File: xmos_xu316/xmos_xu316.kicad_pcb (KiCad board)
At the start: 6 copper layers, 50 x 50 mm, 93 parts, among them CN1 PJ-327A0-SMT, J1 Conn_02x14_Odd_Even, J2 Conn_02x14_Odd_Even, J3 USB_C_Receptacle_USB2.0_16P, U1 XU316-1024-QF60B-C24, U10 SN74AVC4T774PWR, U11 CS43131-CNZR, U12 NZ2520SDA-24.576MHZ, U13 PCA9306DCUR, U2 USB6B1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

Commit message: fixed pcb errors
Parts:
- added R19: 1M, Resistor_SMD:R_0603_1608Metric, F.Cu at (156.0, 87.2)
- C1, C2: value 10pF -> 22pF
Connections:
- J2 pad 2: /xu316/X1D11 -> /xu316/X1D09
- U1 pad 11: MCU_MCLK -> /xu316/X1D09
- U1 pad 14: /xu316/X1D11 -> MCU_MCLK
- U10 pad 3: MCU_MCLK -> /xu316/X1D09
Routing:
- net /xu316/X1D09: track 0.00 -> 67.2 mm, vias 0 -> 2
- net /xu316/X1D11: track 31.2 -> 0.00 mm, vias 1 -> 0
- net MCU_MCLK: track 67.1 -> 36.4 mm, vias 2 -> 1
- net /xu316/HSE_IN: track 7.90 -> 9.88 mm

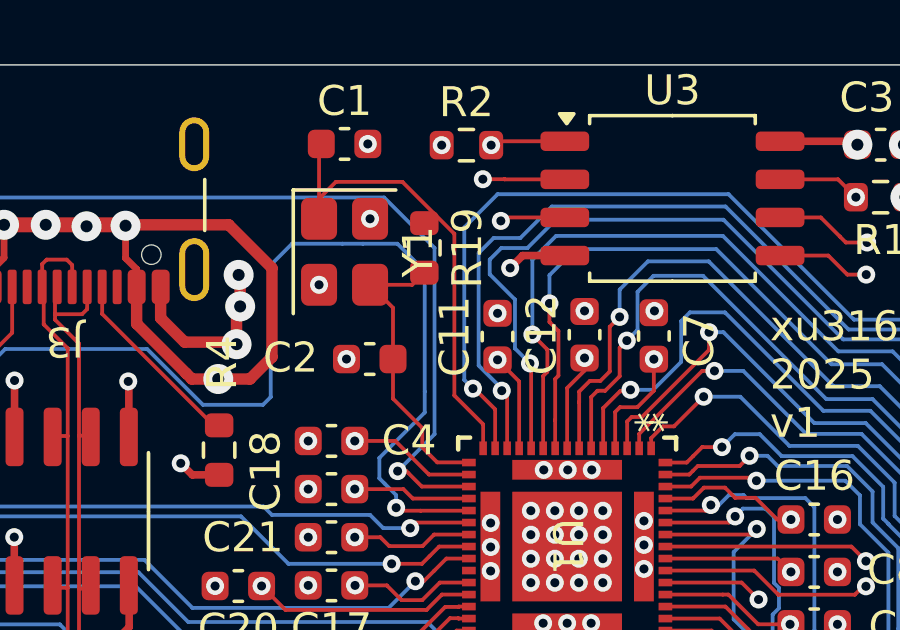
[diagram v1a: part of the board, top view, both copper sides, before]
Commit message: fixed one more error(SN74AVC4T774)
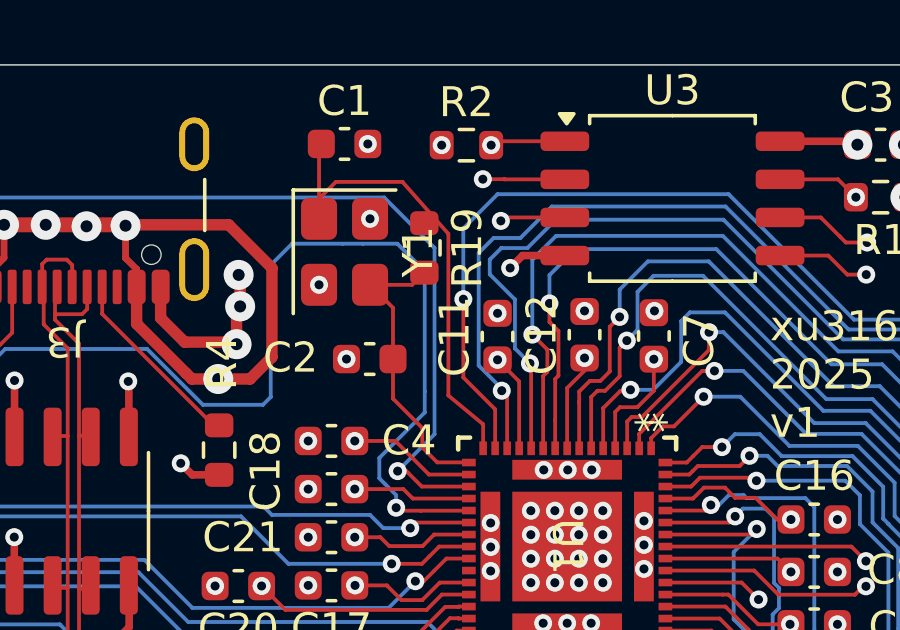
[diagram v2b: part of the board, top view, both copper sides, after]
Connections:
- U10 pad 3: /xu316/X1D09 -> MCU_MCLK
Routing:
- net /xu316/X1D09: track 67.2 -> 29.0 mm, vias 2 -> 1
- net MCU_MCLK: track 36.4 -> 73.3 mm, vias 1 -> 2
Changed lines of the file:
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@@
 			(size 1.778 0.3556)
 			(layers "F.Cu" "F.Mask" "F.Paste")
-			(net 29 "/xu316/X1D09")
+			(net 66 "MCU_MCLK")
 			(pinfunction "A1")
 			(pintype "bidirectional")
@@
 	)
 	(segment
-		(start 157 86.72)
+		(start 156.8 86.72)
 		(end 155.27 84.99)
 		(width 0.127)
@@
 	)
 	(segment
-		(start 157 92.11)
-		(end 157 86.72)
+		(start 156.8 92.11)
+		(end 156.8 86.72)
 		(width 0.127)
 		(layer "F.Cu")
@@
 	(segment
 		(start 157.95935 93.06935)
-		(end 157 92.11)
+		(end 156.8 92.11)
 		(width 0.127)
 		(layer "F.Cu")
@@
 	)
 	(segment
-		(start 138.2688 111.414801)
-		(end 141.465199 111.414801)
-		(width 0.127)
-		(layer "F.Cu")
-		(net 29)
-	)
-	(segment
 		(start 159.55955 91.07955)
 		(end 159.55955 93.870102)
@@
 		(net 29)
 	)
-	(segment
-		(start 141.465199 111.414801)
-		(end 141.55 111.33)
-		(width 0.127)
-		(layer "F.Cu")
-		(net 29)
-	)
 	(via
 		(at 159.52 91.04)
@@
 		(net 29)
 	)
-	(via
-		(at 141.55 111.33)
-		(size 0.6)
-		(drill 0.3)
-		(layers "F.Cu" "B.Cu")
-		(net 29)
-	)
 	(segment
 		(start 159.02 90.54)
@@
 	)
 	(segment
-		(start 146.52 96.87)
-		(end 146.52 109.17)
-		(width 0.127)
-		(layer "In2.Cu")
-		(net 29)
-	)
-	(segment
-		(start 149.39 94)
-		(end 146.52 96.87)
-		(width 0.127)
-		(layer "In2.Cu")
-		(net 29)
-	)
-	(segment
-		(start 149.39 92.81)
-		(end 149.39 94)
-		(width 0.127)
-		(layer "In2.Cu")
-		(net 29)
-	)
-	(segment
-		(start 157.18 90.22)
-		(end 155.71 91.69)
-		(width 0.127)
-		(layer "In2.Cu")
-		(net 29)
-	)
-	(segment
-		(start 158.63 90.22)
-		(end 157.18 90.22)
-		(width 0.127)
-		(layer "In2.Cu")
-		(net 29)
-	)
-	(segment
-		(start 144.36 111.33)
-		(end 141.55 111.33)
-		(width 0.127)
-		(layer "In2.Cu")
-		(net 29)
-	)
-	(segment
 		(start 159.52 91.04)
 		(end 159.45 91.04)
@@
 	)
 	(segment
-		(start 146.52 109.17)
-		(end 144.36 111.33)
-		(width 0.127)
-		(layer "In2.Cu")
-		(net 29)
-	)
-	(segment
-		(start 150.51 91.69)
-		(end 149.39 92.81)
-		(width 0.127)
-		(layer "In2.Cu")
-		(net 29)
-	)
-	(segment
-		(start 155.71 91.69)
-		(end 150.51 91.69)
-		(width 0.127)
-		(layer "In2.Cu")
-		(net 29)
-	)
-	(segment
-		(start 159.45 91.04)
-		(end 158.63 90.22)
-		(width 0.127)
-		(layer "In2.Cu")
-		(net 29)
-	)
-	(segment
 		(start 155.47 94.7)
 		(end 155.4 94.63)
@@
 	)
 	(segment
+		(start 157.3 91.51)
+		(end 157.3 88.9)
+		(width 0.127)
+		(layer "F.Cu")
+		(net 66)
+	)
+	(segment
+		(start 138.2688 111.414801)
+		(end 141.465199 111.414801)
+		(width 0.127)
+		(layer "F.Cu")
+		(net 66)
+	)
+	(segment
 		(start 158.3594 92.5694)
-		(end 158.3594 93.870102)
+		(end 157.3 91.51)
 		(width 0.127)
 		(layer "F.Cu")
@@
 	)
 	(segment
-		(start 157.62 91.88)
-		(end 157.67 91.88)
+		(start 141.465199 111.414801)
+		(end 141.55 111.33)
 		(width 0.127)
 		(layer "F.Cu")
@@
 	)
 	(segment
-		(start 157.67 91.88)
+		(start 158.3594 93.870102)
 		(end 158.3594 92.5694)
 		(width 0.127)
@@
 	)
 	(via
-		(at 157.62 91.88)
+		(at 141.55 111.33)
 		(size 0.6)
 		(drill 0.3)
@@
 		(net 66)
 	)
+	(via
+		(at 157.3 88.9)
+		(size 0.6)
+		(drill 0.3)
+		(layers "F.Cu" "B.Cu")
+		(free yes)
+		(net 66)
+	)
 	(segment
-		(start 178.5 88.1545)
-		(end 178.5 90.82)
+		(start 166.14 85.4)
+		(end 170.32 89.58)
 		(width 0.127)
 		(layer "B.Cu")
@@
 	)
 	(segment
-		(start 178.5 90.82)
-		(end 177.2 92.12)
+		(start 170.32 89.58)
+		(end 172.04 89.58)
 		(width 0.127)
 		(layer "B.Cu")
@@
 	)
 	(segment
-		(start 157.33 86.51)
-		(end 158.44 85.4)
+		(start 174 87.9)
+		(end 178.2455 87.9)
 		(width 0.127)
 		(layer "B.Cu")
@@
 	)
 	(segment
-		(start 157.33 91.59)
-		(end 157.33 86.51)
+		(start 157.3 86.54)
+		(end 158.44 85.4)
 		(width 0.127)
 		(layer "B.Cu")
@@
 	)
 	(segment
-		(start 170.32 89.58)
-		(end 172.04 89.58)
+		(start 172.04 89.58)
+		(end 174 87.9)
 		(width 0.127)
 		(layer "B.Cu")
@@
 	)
 	(segment
-		(start 174 87.9)
-		(end 178.2455 87.9)
+		(start 178.5 88.1545)
+		(end 178.5 90.82)
 		(width 0.127)
 		(layer "B.Cu")
@@
 	)
 	(segment
-		(start 178.2455 87.9)
-		(end 178.5 88.1545)
+		(start 157.3 88.9)
+		(end 157.3 86.54)
 		(width 0.127)
 		(layer "B.Cu")
@@
 	)
 	(segment
-		(start 166.14 85.4)
-		(end 170.32 89.58)
+		(start 178.2455 87.9)
+		(end 178.5 88.1545)
 		(width 0.127)
 		(layer "B.Cu")
@@
 	)
 	(segment
-		(start 157.62 91.88)
-		(end 157.33 91.59)
+		(start 178.5 90.82)
+		(end 177.2 92.12)
 		(width 0.127)
 		(layer "B.Cu")
@@
 	)
 	(segment
-		(start 172.04 89.58)
-		(end 174 87.9)
+		(start 157.3 89.92)
+		(end 157.3 88.9)
 		(width 0.127)
-		(layer "B.Cu")
+		(layer "In2.Cu")
+		(net 66)
+	)
+	(segment
+		(start 146.52 96.87)
+		(end 146.52 109.17)
+		(width 0.127)
+		(layer "In2.Cu")
+		(net 66)
+	)
+	(segment
+		(start 149.39 94)
+		(end 146.52 96.87)
+		(width 0.127)
+		(layer "In2.Cu")
+		(net 66)
+	)
+	(segment
+		(start 149.39 92.81)
+		(end 149.39 94)
+		(width 0.127)
+		(layer "In2.Cu")
+		(net 66)
+	)
+	(segment
+		(start 144.36 111.33)
+		(end 141.55 111.33)
+		(width 0.127)
+		(layer "In2.Cu")
+		(net 66)
+	)
+	(segment
+		(start 146.52 109.17)
+		(end 144.36 111.33)
+		(width 0.127)
+		(layer "In2.Cu")
+		(net 66)
+	)
+	(segment
+		(start 150.51 91.69)
+		(end 149.39 92.81)
+		(width 0.127)
+		(layer "In2.Cu")
+		(net 66)
+	)
+	(segment
+		(start 155.71 91.69)
+		(end 150.51 91.69)
+		(width 0.127)
+		(layer "In2.Cu")
+		(net 66)
+	)
+	(segment
+		(start 155.71 91.69)
+		(end 157.3 89.92)
+		(width 0.127)
+		(layer "In2.Cu")
 		(net 66)
 	)

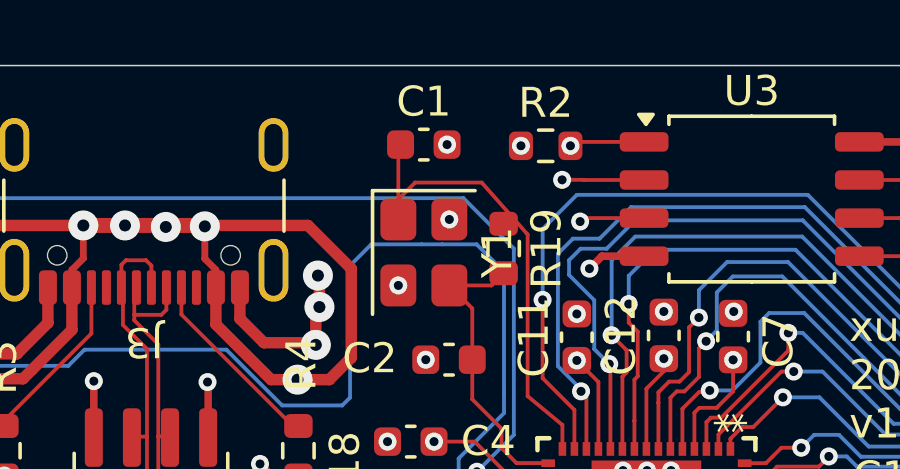
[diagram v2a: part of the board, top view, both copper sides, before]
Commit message: add rd for HSE
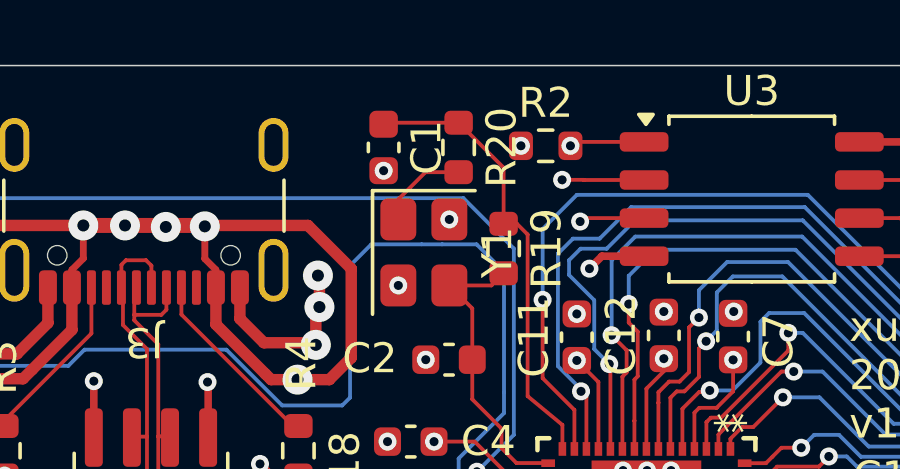
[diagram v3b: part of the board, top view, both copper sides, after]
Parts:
- added R20: 680, Resistor_SMD:R_0603_1608Metric, F.Cu at (154.5, 83.8)
- moved C1 1.34 mm to (152.0, 83.8), turned to -90 degrees
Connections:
- Y1 pad 1: /xu316/HSE_OUT -> Net-(R20-Pad2)
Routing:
- net Net-(R20-Pad2): track 0.00 -> 3.05 mm
- net /xu316/HSE_OUT: track 16.2 -> 15.2 mm
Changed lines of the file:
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@@
 	(net 96 "unconnected-(U11A-DSDCLK{slash}SCLK2-Pad32)")
 	(net 97 "unconnected-(U11A-DDB{slash}LRCK2-Pad29)")
+	(net 98 "Net-(R20-Pad2)")
 	(footprint "Resistor_SMD:R_0603_1608Metric"
 		(layer "F.Cu")
@@
 		)
 	)
+	(footprint "Resistor_SMD:R_0603_1608Metric"
+		(layer "F.Cu")
+		(at 154.5 83.82 -90)
+		(descr "Resistor SMD 0603 (1608 Metric), square (rectangular) end terminal, IPC_7351 nominal, (Body size source: IPC-SM-782 page 72, https://www.pcb-3d.com/wordpress/wp-content/uploads/ipc-sm-782a_amendment_1_and_2.pdf), generated with kicad-footprint-generator")
+		(tags "resistor")
+		(property "Reference" "R20"
+			(at 0 -1.43 90)
+			(layer "F.SilkS")
+			(effects
+				(font
+					(size 1 1)
+					(thickness 0.15)
+				)
+			)
+		)
+		(property "Value" "680"
+			(at 0 1.43 90)
+			(layer "F.Fab")
+			(effects
+				(font
+					(size 1 1)
+					(thickness 0.15)
+				)
+			)
+		)
+		(property "Datasheet" "~"
+			(at 0 0 90)
+			(layer "F.Fab")
+			(hide yes)
+			(effects
+				(font
+					(size 1.27 1.27)
+					(thickness 0.15)
+				)
+			)
+		)
+		(property "Description" "Resistor"
+			(at 0 0 90)
+			(layer "F.Fab")
+			(hide yes)
+			(effects
+				(font
+					(size 1.27 1.27)
+					(thickness 0.15)
+				)
+			)
+		)
+		(property ki_fp_filters "R_*")
+		(sheetname "/xu316/")
+		(sheetfile "xu316.kicad_sch")
+		(attr smd)
+		(fp_line
+			(start -0.237258 0.5225)
+			(end 0.237258 0.5225)
+			(stroke
+				(width 0.12)
+				(type solid)
+			)
+			(layer "F.SilkS")
+		)
+		(fp_line
+			(start -0.237258 -0.5225)
+			(end 0.237258 -0.5225)
+			(stroke
+				(width 0.12)
+				(type solid)
+			)
+			(layer "F.SilkS")
+		)
+		(fp_line
+			(start -1.48 0.73)
+			(end -1.48 -0.73)
+			(stroke
+				(width 0.05)
+				(type solid)
+			)
+			(layer "F.CrtYd")
+		)
+		(fp_line
+			(start 1.48 0.73)
+			(end -1.48 0.73)
+			(stroke
+				(width 0.05)
+				(type solid)
+			)
+			(layer "F.CrtYd")
+		)
+		(fp_line
+			(start -1.48 -0.73)
+			(end 1.48 -0.73)
+			(stroke
+				(width 0.05)
+				(type solid)
+			)
+			(layer "F.CrtYd")
+		)
+		(fp_line
+			(start 1.48 -0.73)
+			(end 1.48 0.73)
+			(stroke
+				(width 0.05)
+				(type solid)
+			)
+			(layer "F.CrtYd")
+		)
+		(fp_line
+			(start -0.8 0.4125)
+			(end -0.8 -0.4125)
+			(stroke
+				(width 0.1)
+				(type solid)
+			)
+			(layer "F.Fab")
+		)
+		(fp_line
+			(start 0.8 0.4125)
+			(end -0.8 0.4125)
+			(stroke
+				(width 0.1)
+				(type solid)
+			)
+			(layer "F.Fab")
+		)
+		(fp_line
+			(start -0.8 -0.4125)
+			(end 0.8 -0.4125)
+			(stroke
+				(width 0.1)
+				(type solid)
+			)
+			(layer "F.Fab")
+		)
+		(fp_line
+			(start 0.8 -0.4125)
+			(end 0.8 0.4125)
+			(stroke
+				(width 0.1)
+				(type solid)
+			)
+			(layer "F.Fab")
+		)
+		(fp_text user "${REFERENCE}"
+			(at 0 0 90)
+			(layer "F.Fab")
+			(effects
+				(font
+					(size 0.4 0.4)
+					(thickness 0.06)
+				)
+			)
+		)
+		(pad "1" smd roundrect
+			(at -0.825 0 270)
+			(size 0.8 0.95)
+			(layers "F.Cu" "F.Mask" "F.Paste")
+			(roundrect_rratio 0.25)
+			(net 10 "/xu316/HSE_OUT")
+			(pintype "passive")
+		)
+		(pad "2" smd roundrect
+			(at 0.825 0 270)
+			(size 0.8 0.95)
+			(layers "F.Cu" "F.Mask" "F.Paste")
+			(roundrect_rratio 0.25)
+			(net 98 "Net-(R20-Pad2)")
+			(pintype "passive")
+		)
+		(embedded_fonts no)
+		(model "${KICAD6_3DMODEL_DIR}/Resistor_SMD.3dshapes/R_0603_1608Metric.wrl"
+			(offset
+				(xyz 0 0 0)
+			)
+			(scale
+				(xyz 1 1 1)
+			)
+			(rotate
+				(xyz 0 0 0)
+			)
+		)
+	)
 	(footprint "Capacitor_SMD:C_0603_1608Metric"
 		(layer "F.Cu")
@@
 	(footprint "Capacitor_SMD:C_0603_1608Metric"
 		(layer "F.Cu")
-		(at 153.34 83.725)
+		(at 152 83.82 -90)
 		(descr "Capacitor SMD 0603 (1608 Metric), square (rectangular) end terminal, IPC-7351 nominal, (Body size source: IPC-SM-782 page 76, https://www.pcb-3d.com/wordpress/wp-content/uploads/ipc-sm-782a_amendment_1_and_2.pdf), generated with kicad-footprint-generator")
 		(tags "capacitor")
 		(property "Reference" "C1"
-			(at 0 -1.43 0)
+			(at 0 -1.43 90)
 			(layer "F.SilkS")
 			(effects
@@
 		)
 		(property "Value" "22pF"
-			(at 0 1.43 0)
+			(at 0 1.43 90)
 			(layer "F.Fab")
 			(effects
@@
 		)
 		(property "Datasheet" "~"
-			(at 0 0 0)
+			(at 0 0 90)
 			(layer "F.Fab")
 			(hide yes)
@@
 		)
 		(property "Description" "Unpolarized capacitor"
-			(at 0 0 0)
+			(at 0 0 90)
 			(layer "F.Fab")
 			(hide yes)
@@
 		(attr smd)
 		(fp_line
-			(start -0.14058 -0.51)
-			(end 0.14058 -0.51)
+			(start -0.14058 0.51)
+			(end 0.14058 0.51)
 			(stroke
 				(width 0.12)
@@
 		)
 		(fp_line
-			(start -0.14058 0.51)
-			(end 0.14058 0.51)
+			(start -0.14058 -0.51)
+			(end 0.14058 -0.51)
 			(stroke
 				(width 0.12)
@@
 		)
 		(fp_line
-			(start -1.48 -0.73)
-			(end 1.48 -0.73)
+			(start -1.48 0.73)
+			(end -1.48 -0.73)
 			(stroke
 				(width 0.05)
@@
 		)
 		(fp_line
-			(start -1.48 0.73)
-			(end -1.48 -0.73)
+			(start 1.48 0.73)
+			(end -1.48 0.73)
 			(stroke
 				(width 0.05)
@@
 		)
 		(fp_line
-			(start 1.48 -0.73)
-			(end 1.48 0.73)
+			(start -1.48 -0.73)
+			(end 1.48 -0.73)
 			(stroke
 				(width 0.05)
@@
 		)
 		(fp_line
-			(start 1.48 0.73)
-			(end -1.48 0.73)
+			(start 1.48 -0.73)
+			(end 1.48 0.73)
 			(stroke
 				(width 0.05)
@@
 		)
 		(fp_line
-			(start -0.8 -0.4)
-			(end 0.8 -0.4)
+			(start -0.8 0.4)
+			(end -0.8 -0.4)
 			(stroke
 				(width 0.1)
@@
 		)
 		(fp_line
-			(start -0.8 0.4)
-			(end -0.8 -0.4)
+			(start 0.8 0.4)
+			(end -0.8 0.4)
 			(stroke
 				(width 0.1)
@@
 		)
 		(fp_line
-			(start 0.8 -0.4)
-			(end 0.8 0.4)
+			(start -0.8 -0.4)
+			(end 0.8 -0.4)
 			(stroke
 				(width 0.1)
@@
 		)
 		(fp_line
-			(start 0.8 0.4)
-			(end -0.8 0.4)
+			(start 0.8 -0.4)
+			(end 0.8 0.4)
 			(stroke
 				(width 0.1)
@@
 		)
 		(fp_text user "${REFERENCE}"
-			(at 0 0 0)
+			(at 0 0 90)
 			(layer "F.Fab")
 			(effects
@@
 		)
 		(pad "1" smd roundrect
-			(at -0.775 0)
+			(at -0.775 0 270)
 			(size 0.9 0.95)
 			(layers "F.Cu" "F.Mask" "F.Paste")
@@
 		)
 		(pad "2" smd roundrect
-			(at 0.775 0)
+			(at 0.775 0 270)
 			(size 0.9 0.95)
 			(layers "F.Cu" "F.Mask" "F.Paste")
@@
 			(layers "F.Cu" "F.Mask" "F.Paste")
 			(roundrect_rratio 0.208333)
-			(net 10 "/xu316/HSE_OUT")
+			(net 98 "Net-(R20-Pad2)")
 			(pinfunction "1")
 			(pintype "passive")
@@
 	)
 	(via
-		(at 154.115 83.725)
+		(at 152 84.595)
 		(size 0.6)
 		(drill 0.3)
 		(layers "F.Cu" "B.Cu")
+		(free yes)
 		(net 1)
 	)
@@
 	)
 	(segment
-		(start 156.8 86.72)
-		(end 155.27 84.99)
+		(start 154.5 82.995)
+		(end 152.05 82.995)
 		(width 0.127)
 		(layer "F.Cu")
@@
 	)
 	(segment
-		(start 156.8 92.11)
-		(end 156.8 86.72)
+		(start 156.445 86.365)
+		(end 156 86.365)
 		(width 0.127)
 		(layer "F.Cu")
@@
 	)
 	(segment
-		(start 157.95935 93.870102)
-		(end 157.95935 93.06935)
+		(start 156.8 92.11)
+		(end 156.8 86.72)
 		(width 0.127)
 		(layer "F.Cu")
@@
 	)
 	(segment
-		(start 155.27 84.99)
-		(end 153.05 84.99)
+		(start 157.95935 93.870102)
+		(end 157.95935 93.06935)
 		(width 0.127)
 		(layer "F.Cu")
@@
 	)
 	(segment
-		(start 152.49 86.22)
-		(end 152.49 83.8)
+		(start 156 84.495)
+		(end 154.5 82.995)
 		(width 0.127)
 		(layer "F.Cu")
@@
 	)
 	(segment
-		(start 153.05 84.99)
-		(end 152.49 85.55)
+		(start 156.8 86.72)
+		(end 156.445 86.365)
 		(width 0.127)
 		(layer "F.Cu")
@@
 	)
 	(segment
-		(start 152.49 83.8)
-		(end 152.565 83.725)
+		(start 156 86.365)
+		(end 156 84.495)
 		(width 0.127)
 		(layer "F.Cu")
@@
 	)
 	(segment
-		(start 152.49 85.55)
-		(end 152.49 86.22)
+		(start 152.05 82.995)
+		(end 152 83.045)
 		(width 0.127)
 		(layer "F.Cu")
@@
 		(net 88)
 	)
+	(segment
+		(start 152.49 85.55)
+		(end 153.395 84.645)
+		(width 0.127)
+		(layer "F.Cu")
+		(net 98)
+	)
+	(segment
+		(start 152.49 86.22)
+		(end 152.49 85.55)
+		(width 0.127)
+		(layer "F.Cu")
+		(net 98)
+	)
+	(segment
+		(start 153.395 84.645)
+		(end 154.5 84.645)
+		(width 0.127)
+		(layer "F.Cu")
+		(net 98)
+	)
 	(zone
